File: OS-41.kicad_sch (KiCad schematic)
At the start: 65 parts, among them J1 Conn_02x03_Counter_Clockwise, J2 Conn_01x02_Pin, J3 Conn_01x02_Pin, J4 Conn_Coaxial, SW4 SW_Push, U1 BME280, U2 SI4432-B1-FMR, U3 MCP1640x-xCHY, U4 ATGM336H-5N31, U7 STM32F103C8Tx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

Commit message: Routed first version!
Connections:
- net LED_ERR: now also U7.39 (PB3)
- net LED_OK: now also U7.40 (PB4)
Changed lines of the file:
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@@
+		)
+	)
+	(global_label "LED_ERR"
+		(shape input)
+		(at 290.83 91.44 180)
+		(fields_autoplaced yes)
+		(effects
+			(font
+				(size 1.27 1.27)
+			)
+			(justify right)
+		)
+		(property "Intersheetrefs" "${INTERSHEET_REFS}"
+			(at 279.7411 91.44 0)
+			(effects
+				(font
+					(size 1.27 1.27)
+				)
+				(justify right)
+				(hide yes)
+			)
 		)
 	)
@@
 			(effects
 				(font
+					(size 1.27 1.27)
+				)
+				(justify right)
+				(hide yes)
+			)
+		)
+	)
+	(global_label "LED_OK"
+		(shape input)
+		(at 290.83 93.98 180)
+		(fields_autoplaced yes)
+		(effects
+			(font
+				(size 1.27 1.27)
+			)
+			(justify right)
+		)
+		(property "Intersheetrefs" "${INTERSHEET_REFS}"
+			(at 280.8296 93.98 0)
+			(effects
+				(font

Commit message: More routing!
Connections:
- net VCC: no longer J1.4 (Pin_4)
- net PA15: now reaches U7.38 (PA15)
- net PA15: now also J1.4 (Pin_4)
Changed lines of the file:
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@@
+		)
+	)
+	(global_label "PA15"
+		(shape bidirectional)
+		(at 361.95 115.57 0)
+		(effects
+			(font
+				(size 1.27 1.27)
+			)
+			(justify left)
+		)
+		(property "Intersheetrefs" "${INTERSHEET_REFS}"
+			(at 361.95 115.57 0)
+			(effects
+				(font
+					(size 1.27 1.27)
+				)
+				(hide yes)
+			)
 		)
 	)
@@
 		)
 	)
-	(global_label "VCC"
-		(shape input)
-		(at 361.95 115.57 0)
-		(fields_autoplaced yes)
-		(effects
-			(font
-				(size 1.27 1.27)
-			)
-			(justify left)
-		)
-		(property "Intersheetrefs" "${INTERSHEET_REFS}"
-			(at 368.5638 115.57 0)
-			(effects
-				(font
-					(size 1.27 1.27)
-				)
-				(justify left)
-				(hide yes)
-			)
-		)
-	)
 	(global_label "SCL"
 		(shape input)
@@
 				(hide yes)
 			)
+		)
+	)
+	(global_label "PA15"
+		(shape bidirectional)
+		(at 326.39 93.98 0)
+		(effects
+			(font
+				(size 1.27 1.27)
+			)
+			(justify left)
+		)
+		(property "Intersheetrefs" "${INTERSHEET_REFS}"
+			(at 326.39 93.98 0)
+			(effects
+				(font
+					(size 1.27 1.27)
+				)
+				(hide yes)
+			)

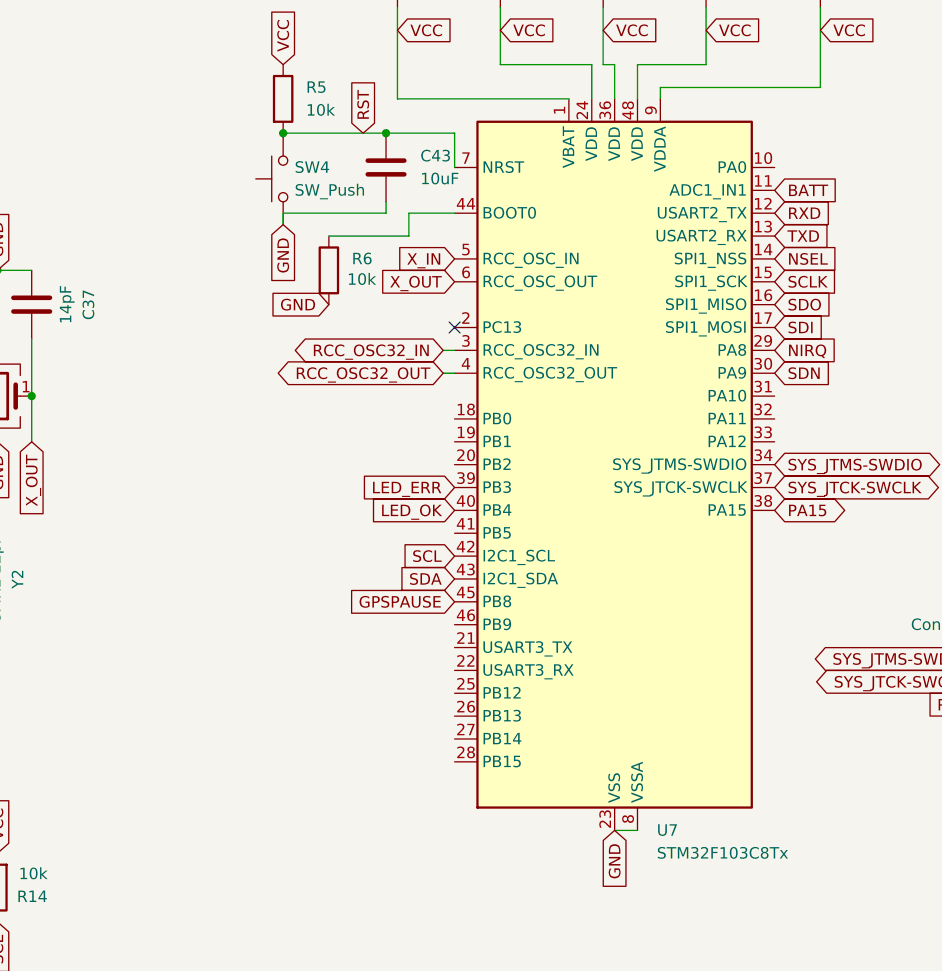
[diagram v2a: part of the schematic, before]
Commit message: Add GPIO breakouts
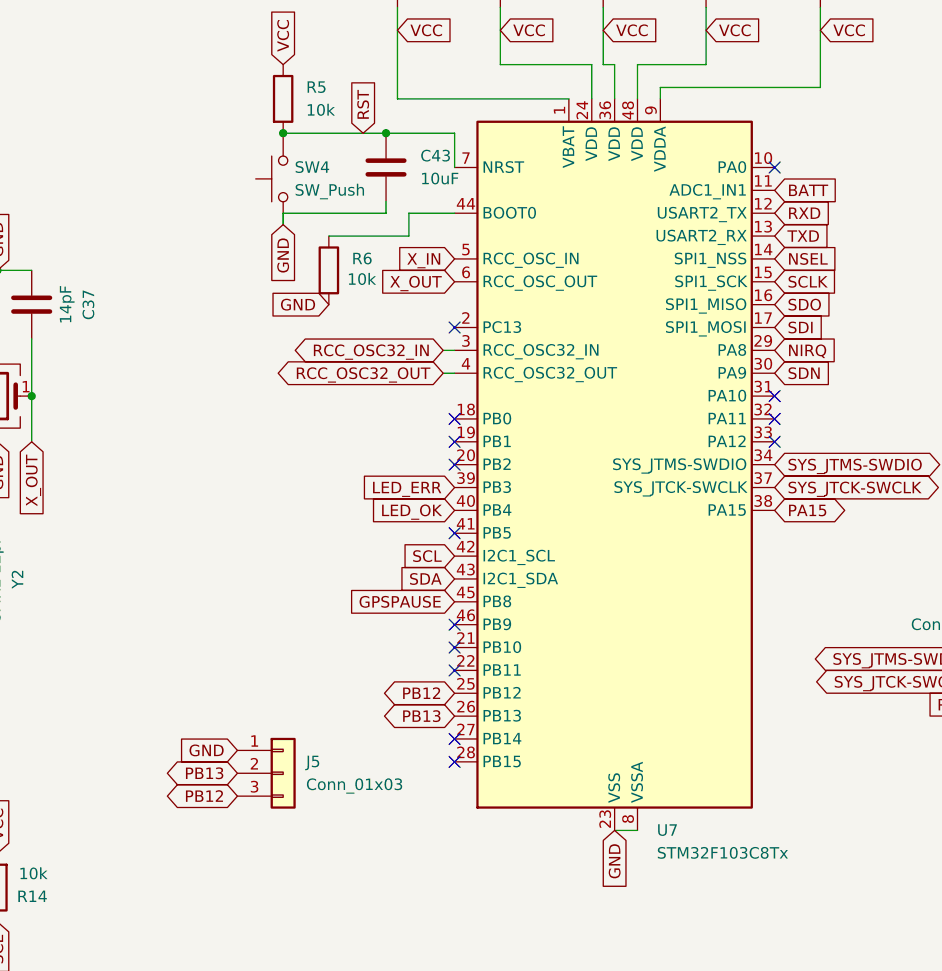
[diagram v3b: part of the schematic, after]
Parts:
- added J5: Conn_01x03, Connector_PinHeader_2.54mm:PinHeader_1x03_P2.54mm_Vertical, symbol Connector_Generic:Conn_01x03
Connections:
- net GND: now also J5.1 (Pin_1)
- net PB12: now reaches U7.25 (PB12)
- net PB12: now also J5.3 (Pin_3)
- net PB13: now reaches U7.26 (PB13)
- net PB13: now also J5.2 (Pin_2)
- no-connect marks 17 -> 30
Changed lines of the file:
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@@
 	)
 	(no_connect
+		(at 326.39 55.88)
+	)
+	(no_connect
 		(at 290.83 73.66)
 	)
 	(no_connect
+		(at 326.39 81.28)
+	)
+	(no_connect
+		(at 290.83 88.9)
+	)
+	(no_connect
 		(at 72.39 147.32)
 	)
 	(no_connect
+		(at 326.39 83.82)
+	)
+	(no_connect
 		(at 96.52 48.26)
 	)
@@
 	)
 	(no_connect
+		(at 290.83 121.92)
+	)
+	(no_connect
+		(at 290.83 119.38)
+	)
+	(no_connect
 		(at 72.39 152.4)
 	)
@@
 	)
 	(no_connect
+		(at 290.83 111.76)
+	)
+	(no_connect
+		(at 290.83 106.68)
+	)
+	(no_connect
 		(at 96.52 45.72)
 	)
@@
 	)
 	(no_connect
+		(at 290.83 96.52)
+	)
+	(no_connect
 		(at 87.63 170.18)
 	)
@@
 	)
 	(no_connect
+		(at 326.39 86.36)
+	)
+	(no_connect
 		(at 72.39 149.86)
 	)
 	(no_connect
+		(at 290.83 83.82)
+	)
+	(no_connect
 		(at 96.52 53.34)
 	)
@@
 		(at 63.5 58.42)
 	)
+	(no_connect
+		(at 290.83 86.36)
+	)
+	(no_connect
+		(at 290.83 109.22)
+	)
 	(wire
 		(pts
@@
 		)
 	)
+	(global_label "PB12"
+		(shape bidirectional)
+		(at 290.83 114.3 180)
+		(effects
+			(font
+				(size 1.27 1.27)
+			)
+			(justify right)
+		)
+		(property "Intersheetrefs" "${INTERSHEET_REFS}"
+			(at 290.83 114.3 0)
+			(effects
+				(font
+					(size 1.27 1.27)
+				)
+				(hide yes)
+			)
+		)
+	)
 	(global_label "GPSPAUSE"
 		(shape input)
@@
 	(global_label "GND"
 		(shape input)
+		(at 266.7 120.65 180)
+		(effects
+			(font
+				(size 1.27 1.27)
+			)
+			(justify right)
+		)
+		(property "Intersheetrefs" "${INTERSHEET_REFS}"
+			(at 266.7 120.65 90)
+			(effects
+				(font
+					(size 1.27 1.27)
+				)
+				(hide yes)
+			)
+		)
+	)
+	(global_label "GND"
+		(shape input)
 		(at 40.64 247.65 180)
 		(fields_autoplaced yes)
@@
 		)
 	)
+	(global_label "PB12"
+		(shape bidirectional)
+		(at 266.7 125.73 180)
+		(effects
+			(font
+				(size 1.27 1.27)
+			)
+			(justify right)
+		)
+		(property "Intersheetrefs" "${INTERSHEET_REFS}"
+			(at 266.7 125.73 0)
+			(effects
+				(font
+					(size 1.27 1.27)
+				)
+				(hide yes)
+			)
+		)
+	)
 	(global_label "LED_OK"
 		(shape input)
@@
 		)
 	)
+	(global_label "PB13"
+		(shape bidirectional)
+		(at 290.83 116.84 180)
+		(effects
+			(font
+				(size 1.27 1.27)
+			)
+			(justify right)
+		)
+		(property "Intersheetrefs" "${INTERSHEET_REFS}"
+			(at 290.83 116.84 0)
+			(effects
+				(font
+					(size 1.27 1.27)
+				)
+				(hide yes)
+			)
+		)
+	)
 	(global_label "BATT"
 		(shape input)
@@
 		)
 	)
+	(global_label "PB13"
+		(shape bidirectional)
+		(at 266.7 123.19 180)
+		(effects
+			(font
+				(size 1.27 1.27)
+			)
+			(justify right)
+		)
+		(property "Intersheetrefs" "${INTERSHEET_REFS}"
+			(at 266.7 123.19 0)
+			(effects
+				(font
+					(size 1.27 1.27)
+				)
+				(hide yes)
+			)
+		)
+	)
 	(global_label "VCC"
 		(shape input)
@@
 		)
 		(pin "22"
-			(alternate "USART3_RX")
 		)
 		(pin "28"
@@
 		)
 		(pin "21"
-			(alternate "USART3_TX")
 		)
 		(pin "23"
@@
 					(unit 1)
 				)
+			)
+		)
+	)
+	(symbol
+		(lib_id "Connector_Generic:Conn_01x03")
+		(at 271.78 123.19 0)
+		(unit 1)
+		(exclude_from_sim no)
+		(in_bom yes)
+		(on_board yes)
+		(dnp no)
+		(fields_autoplaced yes)
+		(property "Reference" "J5"
+			(at 274.32 121.9199 0)
+			(effects
+				(font
+					(size 1.27 1.27)
+				)
+				(justify left)
+			)
+		)
+		(property "Value" "Conn_01x03"
+			(at 274.32 124.4599 0)
+			(effects
+				(font
+					(size 1.27 1.27)
+				)
+				(justify left)
+			)
+		)
+		(property "Footprint" "Connector_PinHeader_2.54mm:PinHeader_1x03_P2.54mm_Vertical"
+			(at 271.78 123.19 0)
+			(effects
+				(font
+					(size 1.27 1.27)
+				)
+				(hide yes)
+			)
+		)
+		(property "Datasheet" "~"
+			(at 271.78 123.19 0)
+			(effects
+				(font
+					(size 1.27 1.27)
+				)
+				(hide yes)
+			)
+		)
+		(property "Description" "Generic connector, single row, 01x03, script generated (kicad-library-utils/schlib/autogen/connector/)"
+			(at 271.78 123.19 0)
+			(effects
+				(font
+					(size 1.27 1.27)
+				)
+				(hide yes)
+			)
+		)
+		(pin "2"
+		)
+		(pin "3"
+		)
+		(pin "1"
+		)
+		(instances
+			(project ""
+				(path "/d2225c9f-058e-4f40-b93c-9ee01fd58030"
+					(reference "J5")
+					(unit 1)
+				)

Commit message: FINALLY found the button footprint...
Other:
- note added: "C51927445"
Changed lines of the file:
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@@
+		)
+	)
+	(text "C51927445"
+		(exclude_from_sim no)
+		(at 260.604 58.166 0)
+		(effects
+			(font
+				(size 1.27 1.27)
+			)
 		)
 	)

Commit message: add notice
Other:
- note added: "NOTE TO SELF: this inductor is currently out of stock - switch footprint to a different one"
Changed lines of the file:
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@@
+		)
+	)
+	(text "NOTE TO SELF: this inductor is currently out of stock - switch footprint to a different one"
+		(exclude_from_sim no)
+		(at 96.266 221.996 0)
+		(effects
+			(font
+				(size 0.254 0.254)
+			)
 		)
 	)
